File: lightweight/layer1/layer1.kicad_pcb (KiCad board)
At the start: 2 copper layers, 208 x 198.4 mm, 228 parts, among them J1 XT30-F, J10 Conn_01x02_Pin, J11 Conn_01x01_Socket, J12 Conn_01x01_Socket, J13 SH1.0 5P, J14 SH1.0 3P, J15 Conn_01x01_Socket, J2 Conn_01x01_Socket, J3 Conn_01x01_Socket, J4 XT30PW-F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

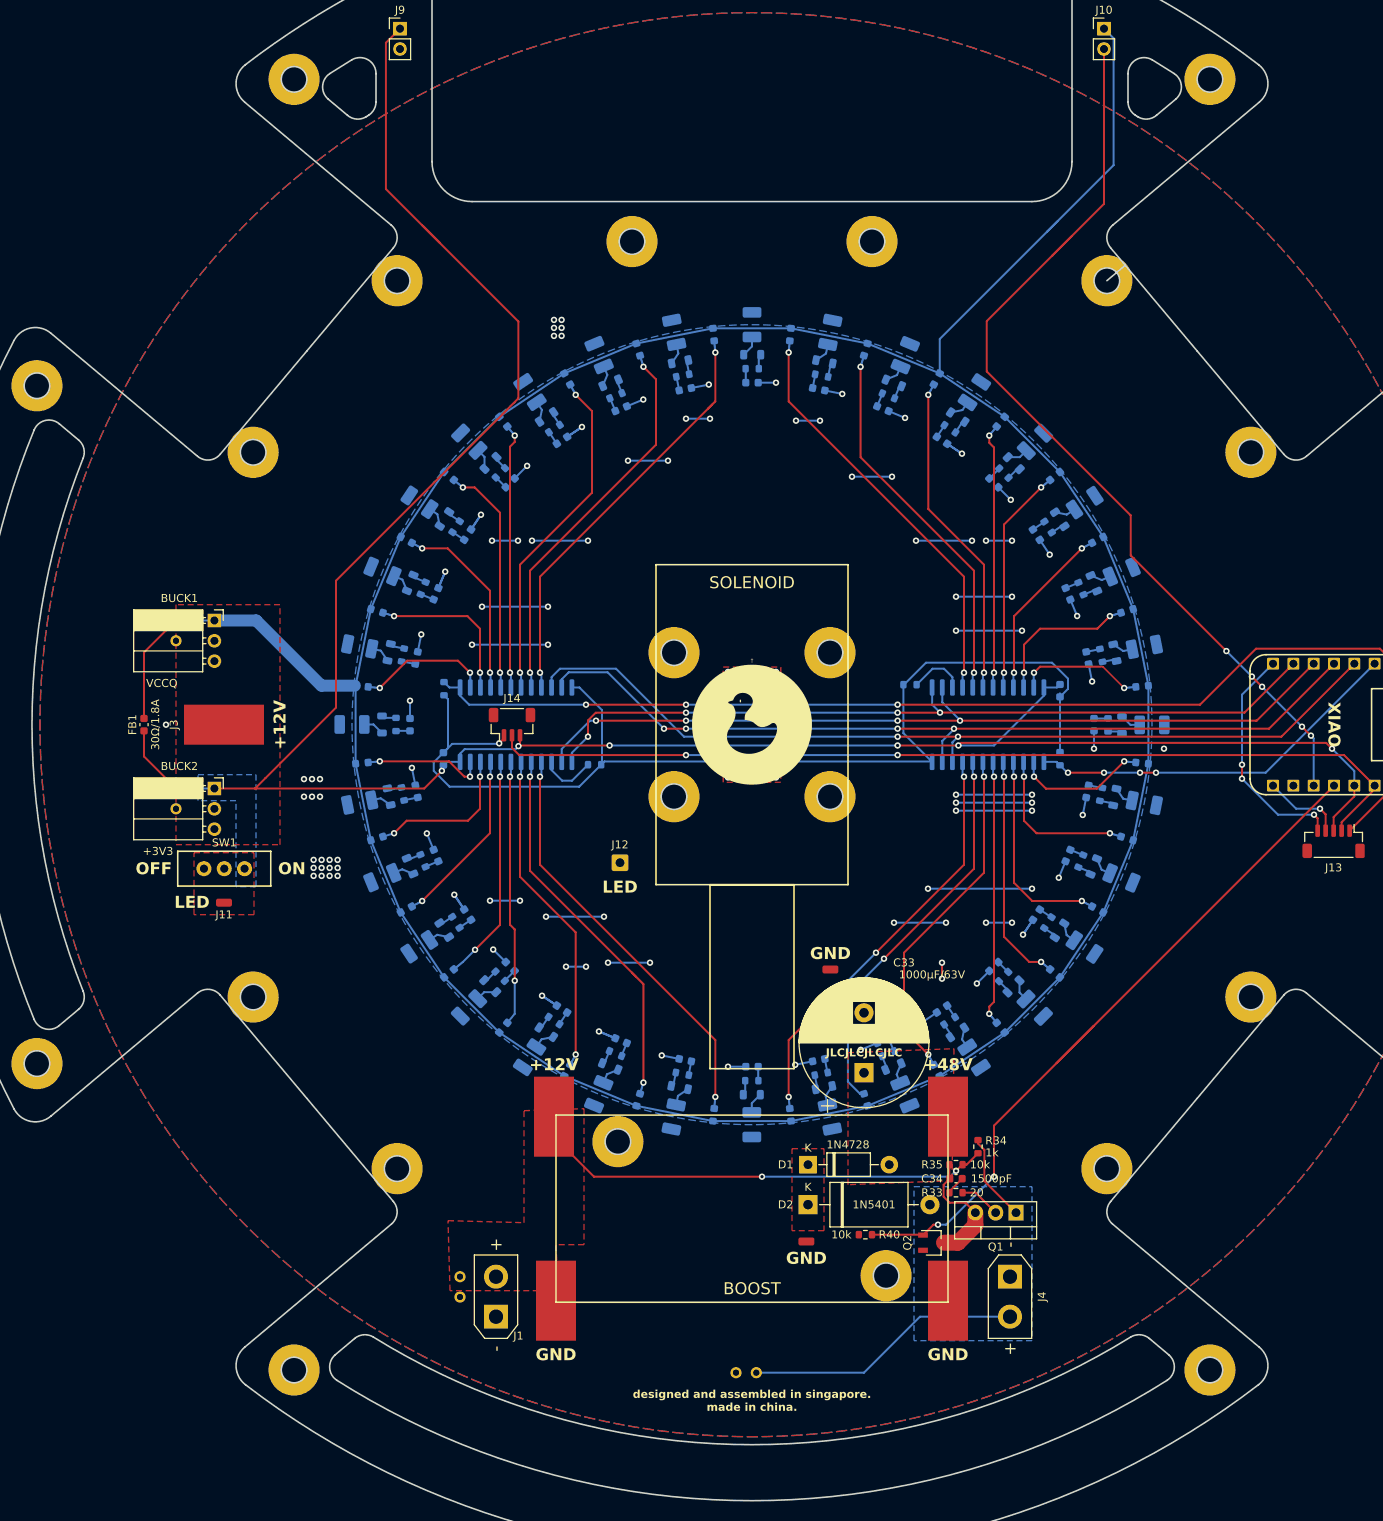
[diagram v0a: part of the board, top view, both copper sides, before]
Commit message: layer 1 lw pcb
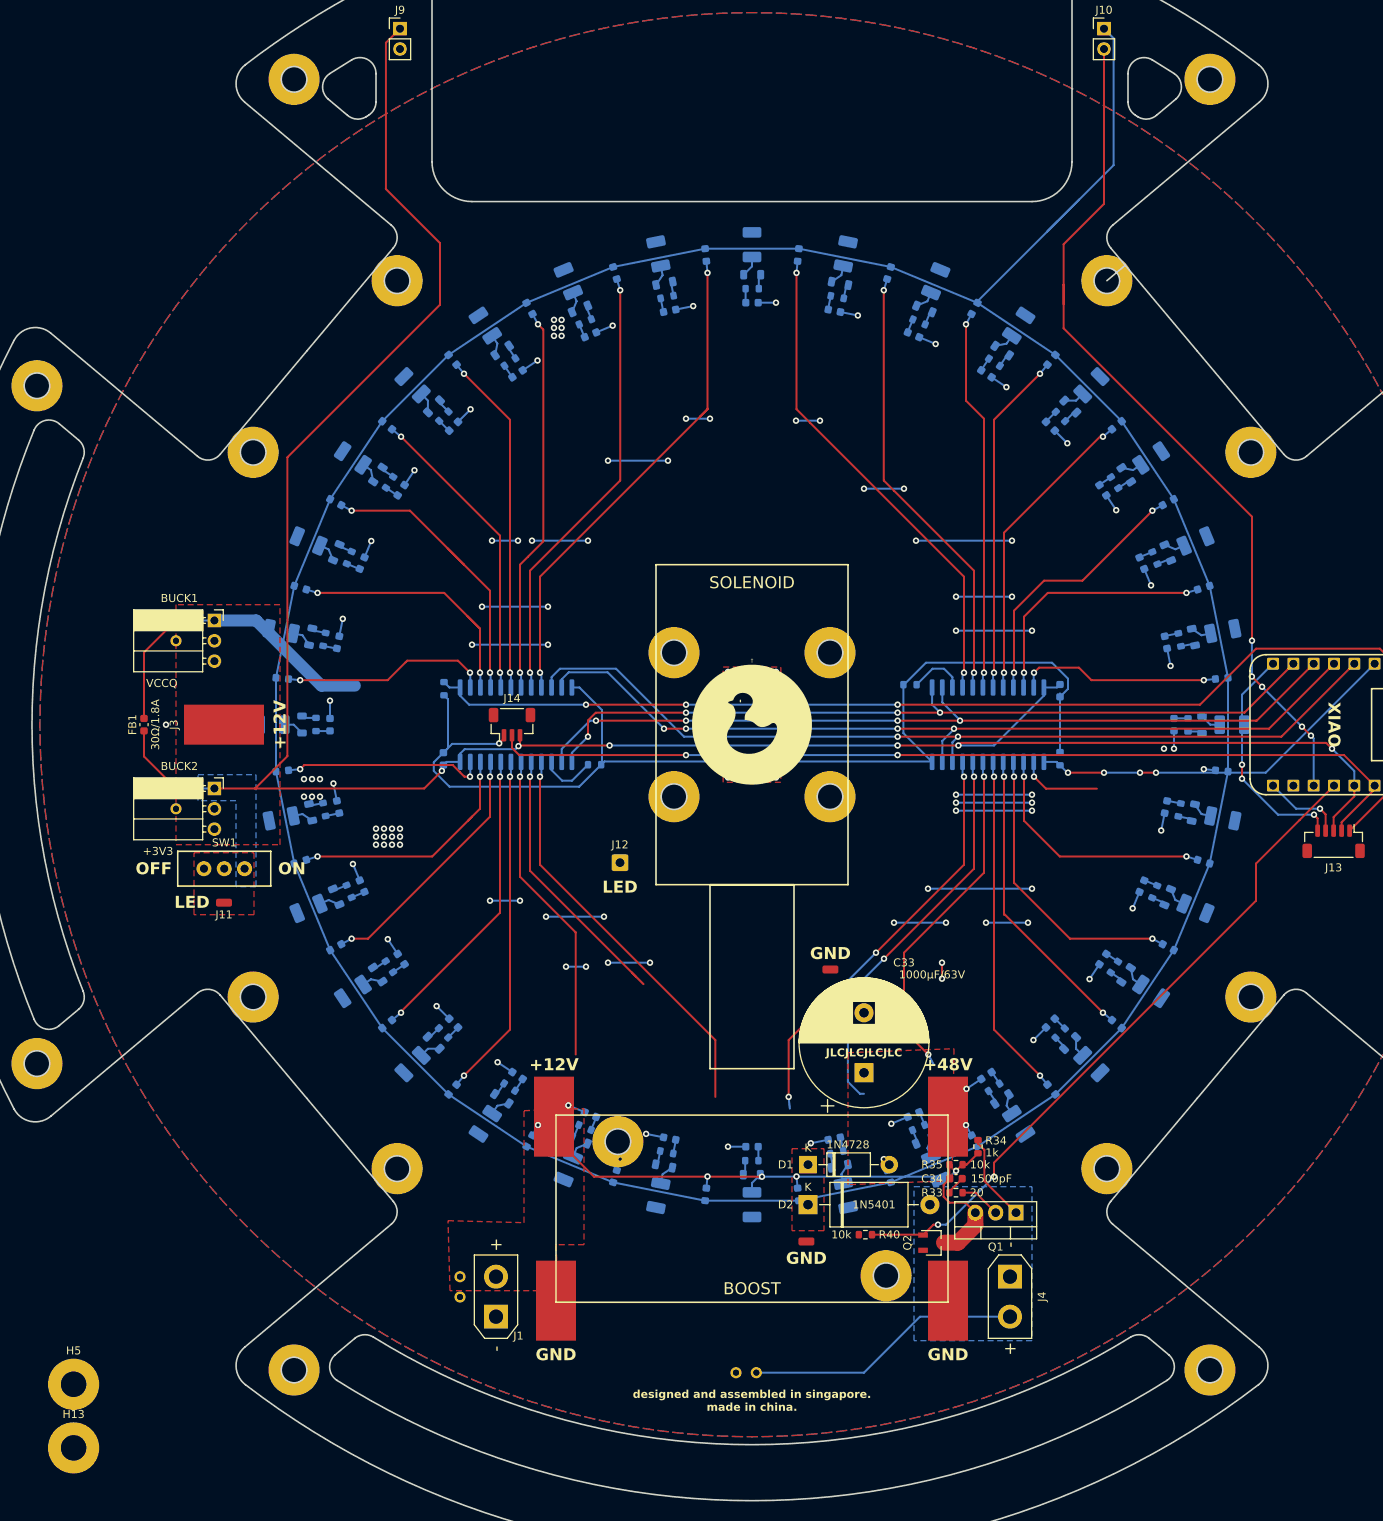
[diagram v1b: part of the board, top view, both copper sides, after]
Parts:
- moved H5 174.3 mm to (20.2, 187.4)
- moved H13 166.2 mm to (20.2, 195.4)
- moved LDR12 10.0 mm to (59.4, 142.4)
- moved LDR4 10.0 mm to (67.6, 59.4)
- moved LDR20 10.0 mm to (142.4, 150.6)
- moved LDR28 10.0 mm to (150.6, 67.6)
- moved LDR3 10.0 mm to (77.2, 53.0)
- moved LDR11 10.0 mm to (53.0, 132.8)
- moved LDR27 10.0 mm to (157.0, 77.2)
- moved LDR19 10.0 mm to (132.8, 157.0)
- moved LDR18 10.0 mm to (122.1, 161.5)
- moved LDR26 10.0 mm to (161.5, 87.9)
- moved LDR10 10.0 mm to (48.5, 122.1)
- moved LDR2 10.0 mm to (87.9, 48.5)
- moved LDR13 10.0 mm to (67.6, 150.6)
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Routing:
- net VCCQ: track 406.4 -> 463.9 mm
- net Net-(U1-I0): track 55.2 -> 72.2 mm, vias 2 -> 8
- net Net-(U1-I14): track 51.0 -> 37.2 mm
- net Net-(U2-I9): track 20.5 -> 33.4 mm
- net Net-(U1-I5): track 25.7 -> 37.9 mm
- net Net-(U1-I6): track 21.7 -> 33.2 mm
- net Net-(U1-I9): track 19.3 -> 30.8 mm
- net +3V3: track 306.6 -> 295.4 mm
- net GND: track 228.7 -> 218.2 mm, vias 102 -> 100
- net /SOLENOIDON: track 95.1 -> 84.8 mm
- net Net-(U1-I3): track 34.7 -> 44.9 mm
- net Net-(U2-I4): track 30.8 -> 40.9 mm
- net Net-(U1-I12): track 33.2 -> 43.1 mm
- net Net-(U2-I10): track 23.9 -> 33.6 mm
- net Net-(U2-I6): track 21.7 -> 31.0 mm
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- removed copper zone on B.Cu, net /LED
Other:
- outline, holes or cut-outs redrawn

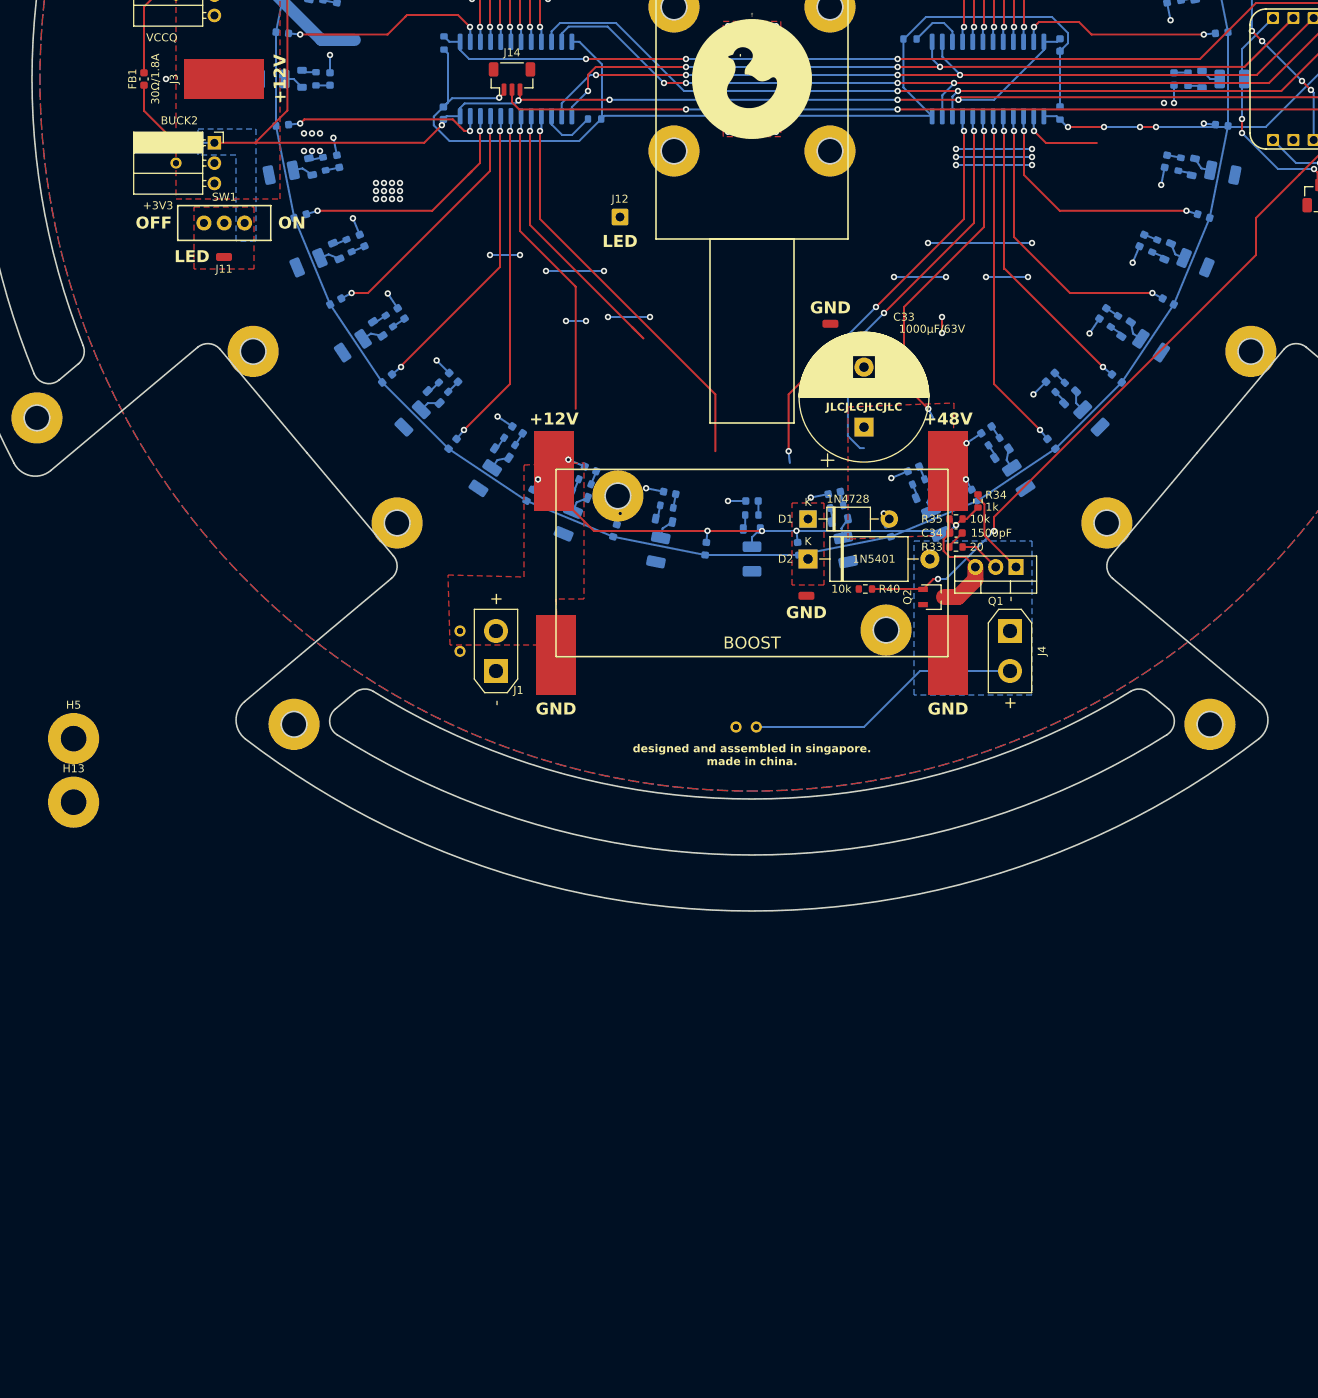
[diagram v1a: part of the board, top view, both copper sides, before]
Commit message: moved boost cirvcuit on lw layer 1
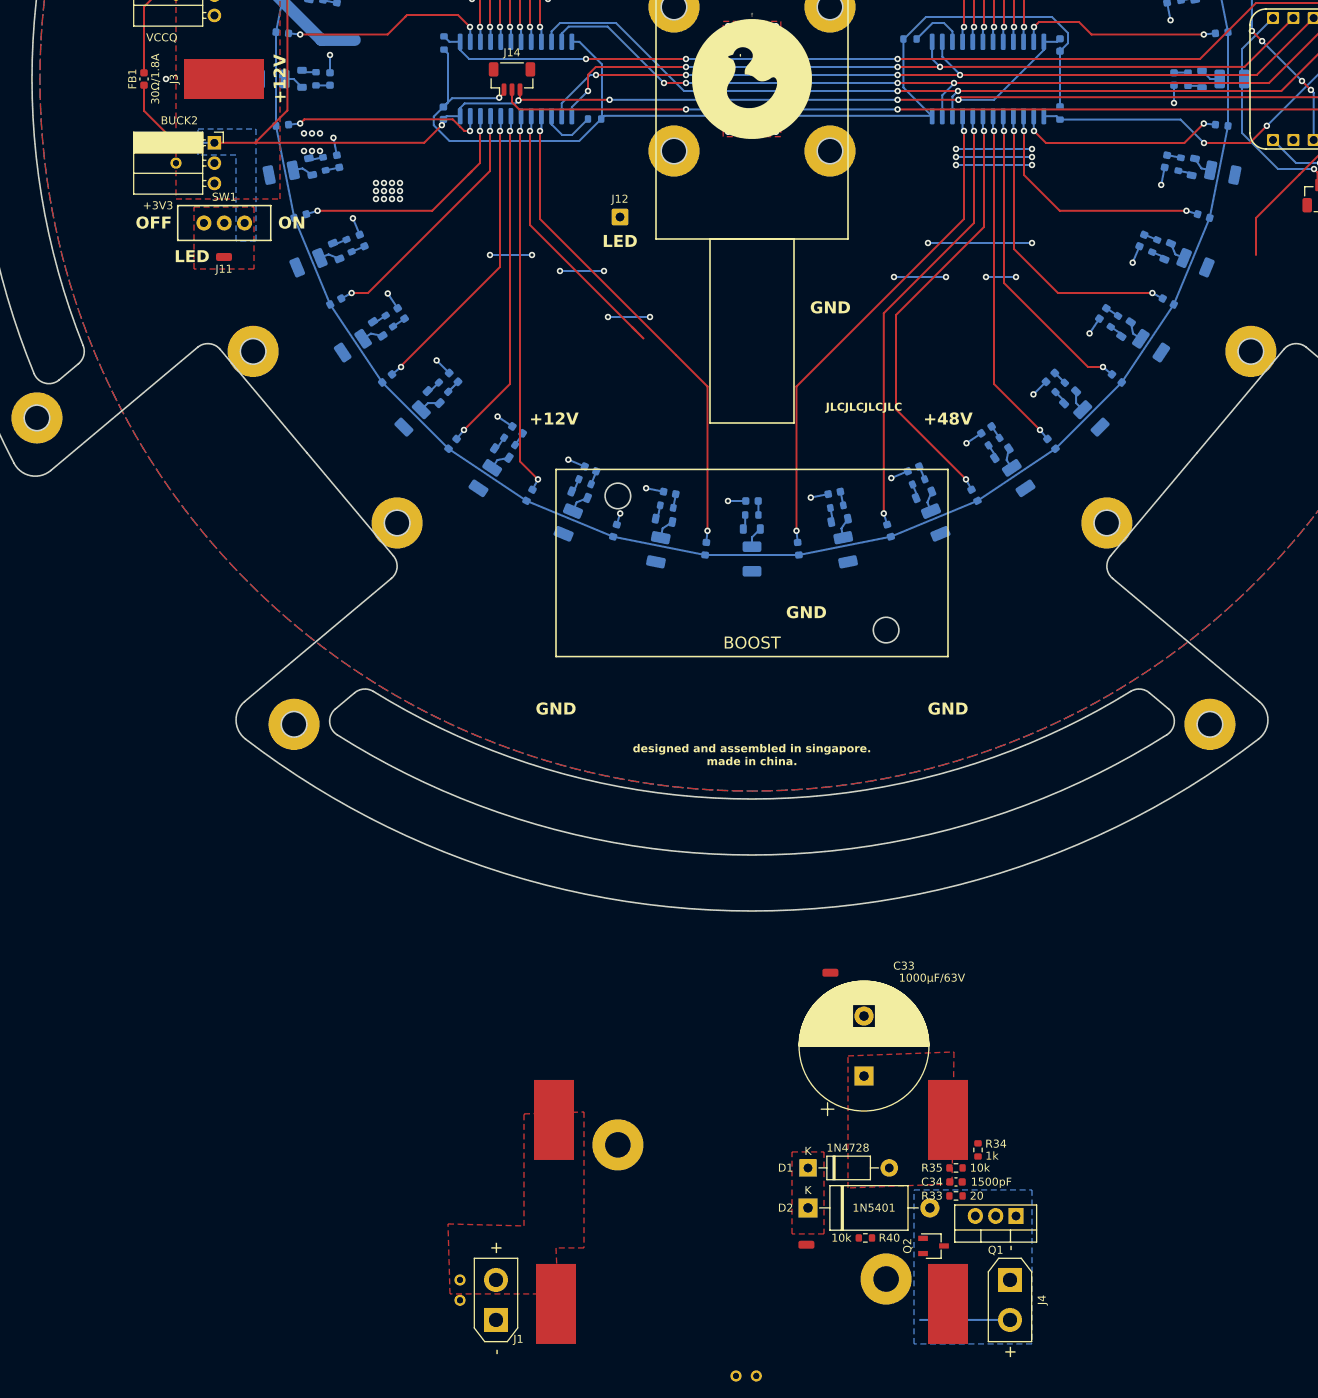
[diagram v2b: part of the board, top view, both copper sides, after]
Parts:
- removed H13, H5: MountingHole, MountingHole:MountingHole_3.2mm_M3_Pad
- moved C33 81.1 mm to (119.0, 229.6)
- moved C34 81.1 mm to (130.5, 242.9)
- moved D1 81.1 mm to (112.0, 241.1)
- moved D2 81.1 mm to (112.0, 246.1)
- moved H23 81.1 mm to (88.2, 238.2)
- moved H24 81.1 mm to (121.8, 255.0)
- moved J1 81.1 mm to (73.0, 260.1)
- moved J15 81.1 mm to (111.8, 250.7)
- moved J2 81.1 mm to (114.8, 216.7)
- moved J4 81.1 mm to (137.2, 255.1)
- moved J5 81.1 mm to (80.2, 235.1)
- moved J6 81.1 mm to (80.5, 258.1)
- moved J7 81.1 mm to (129.5, 235.1)
- moved J8 81.1 mm to (129.5, 258.1)
- moved Q1 81.1 mm to (138.0, 247.1)
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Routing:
- net /SOLENOIDON: track 84.8 -> 18.4 mm, vias 2 -> 0
- net +12V: track 58.8 -> 0.00 mm, vias 2 -> 0
- net +48V: track 34.6 -> 11.2 mm
- net Net-(U2-I7): track 10.3 -> 26.2 mm, vias 1 -> 2
- net Net-(Q1-S): track 15.5 -> 0.00 mm
- net Net-(Q1-G): track 11.0 -> 0.00 mm
- net Net-(U1-I15): track 51.0 -> 62.0 mm, vias 1 -> 2
- net Net-(U2-I2): track 45.0 -> 55.1 mm
- net Net-(U1-I13): track 39.5 -> 48.3 mm, vias 1 -> 2
- net Net-(U1-I0): track 72.2 -> 63.4 mm, vias 8 -> 2
- net Net-(U2-I0): track 54.0 -> 62.0 mm, vias 4 -> 2
- net Net-(U2-I1): track 49.2 -> 55.9 mm
- net Net-(LED1-A): track 7.93 -> 2.64 mm
- net Net-(D2-A): track 5.17 -> 0.00 mm
- net GND: track 218.2 -> 214.0 mm, vias 100 -> 97
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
